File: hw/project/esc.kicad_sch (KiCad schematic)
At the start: 0 parts

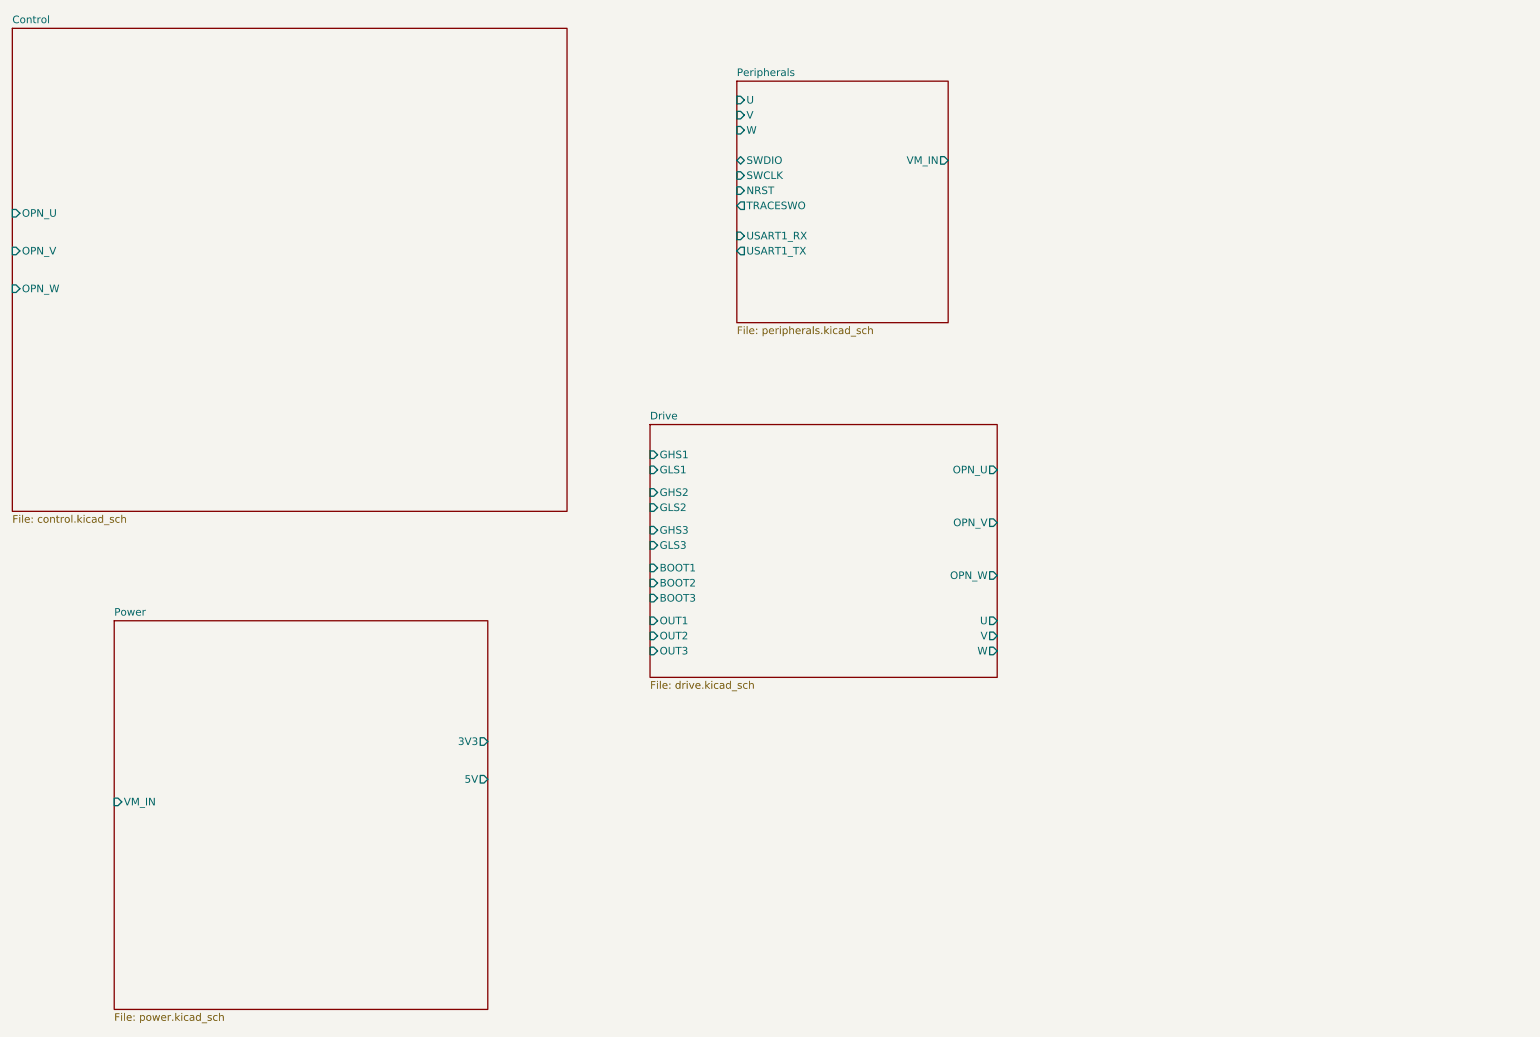
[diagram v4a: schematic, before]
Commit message: added peripherals main sheet and fixed erc errors
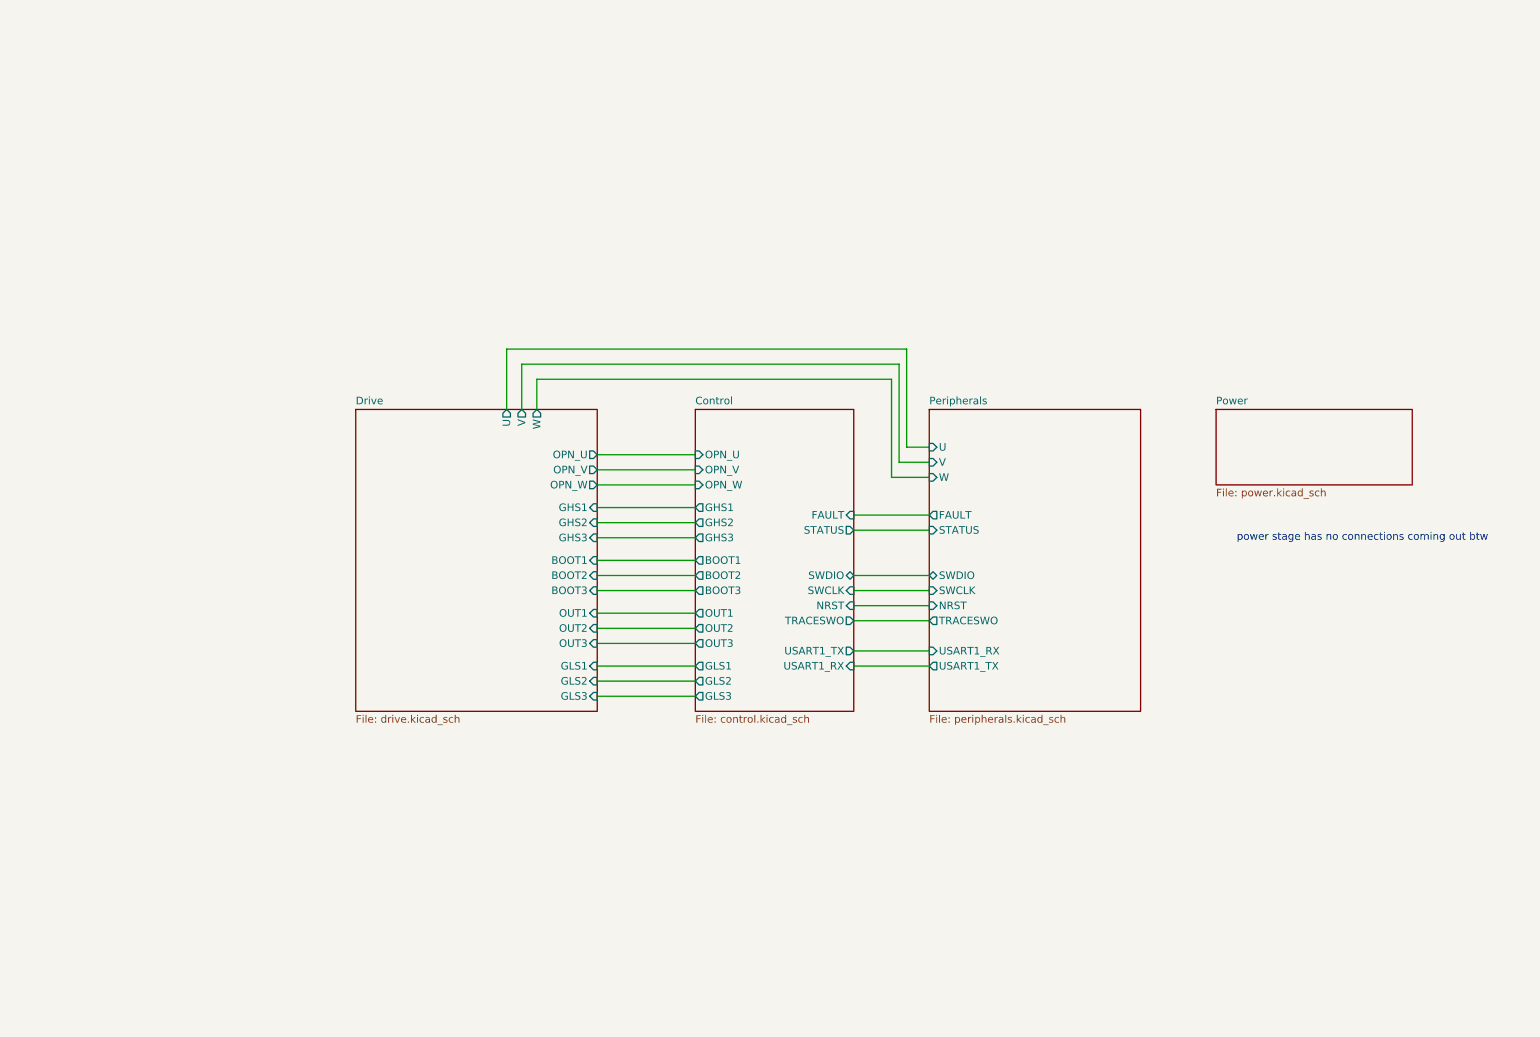
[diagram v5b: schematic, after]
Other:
- sheet Control ports: added BOOT1, BOOT2, BOOT3, FAULT, GHS1, GHS2, GHS3, GLS1, GLS2, GLS3, NRST, OUT1, OUT2, OUT3, STATUS, SWCLK, SWDIO, TRACESWO, USART1_RX, USART1_TX; removed none
- sheet Peripherals ports: added FAULT, STATUS; removed VM_IN
- sheet Power ports: added none; removed 3V3, 5V, VM_IN
- note added: "power stage has no connections coming out btw"

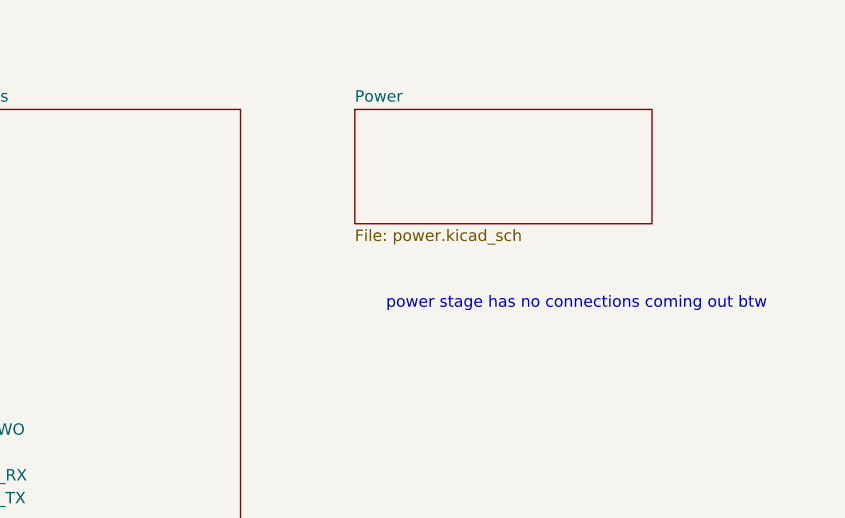
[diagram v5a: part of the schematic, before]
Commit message: Distinguish between hierarchical VM_IN and global VM
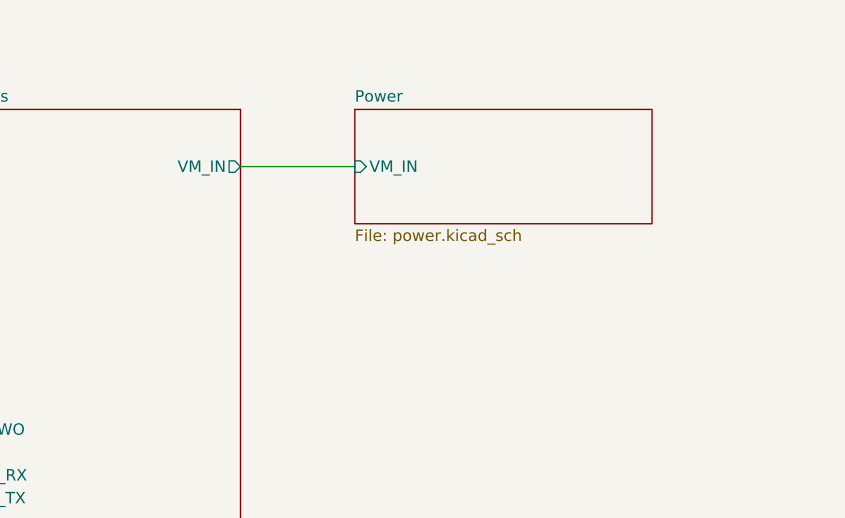
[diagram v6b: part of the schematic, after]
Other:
- sheet Peripherals ports: added VM_IN; removed none
- sheet Power ports: added VM_IN; removed none
- note removed: "power stage has no connections coming out btw"
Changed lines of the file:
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@@
 	(generator_version "10.0")
 	(paper "A4")
-	(text "power stage has no connections coming out btw"
-		(exclude_from_sim no)
-		(at 240.538 101.6 0)
-		(effects
-			(font
-				(size 1.27 1.27)
-			)
-		)
-	)
 	(wire
 		(pts
@@
 		(pts
 			(xy 163.83 69.85) (xy 163.83 86.36)
+		)
+		(stroke
+			(width 0)
+			(type default)
+		)
+	)
+	(wire
+		(pts
+			(xy 203.2 86.36) (xy 215.9 86.36)
 		)
 		(stroke
@@
 			)
 		)
+		(pin "VM_IN" input
+			(at 215.9 86.36 180)
+			(effects
+				(font
+					(size 1.27 1.27)
+				)
+				(justify left)
+			)
+		)
 		(instances
 			(project "esc"
@@
 			)
 		)
+		(pin "VM_IN" output
+			(at 203.2 86.36 0)
+			(effects
+				(font
+					(size 1.27 1.27)
+				)
+				(justify right)
+			)
+		)

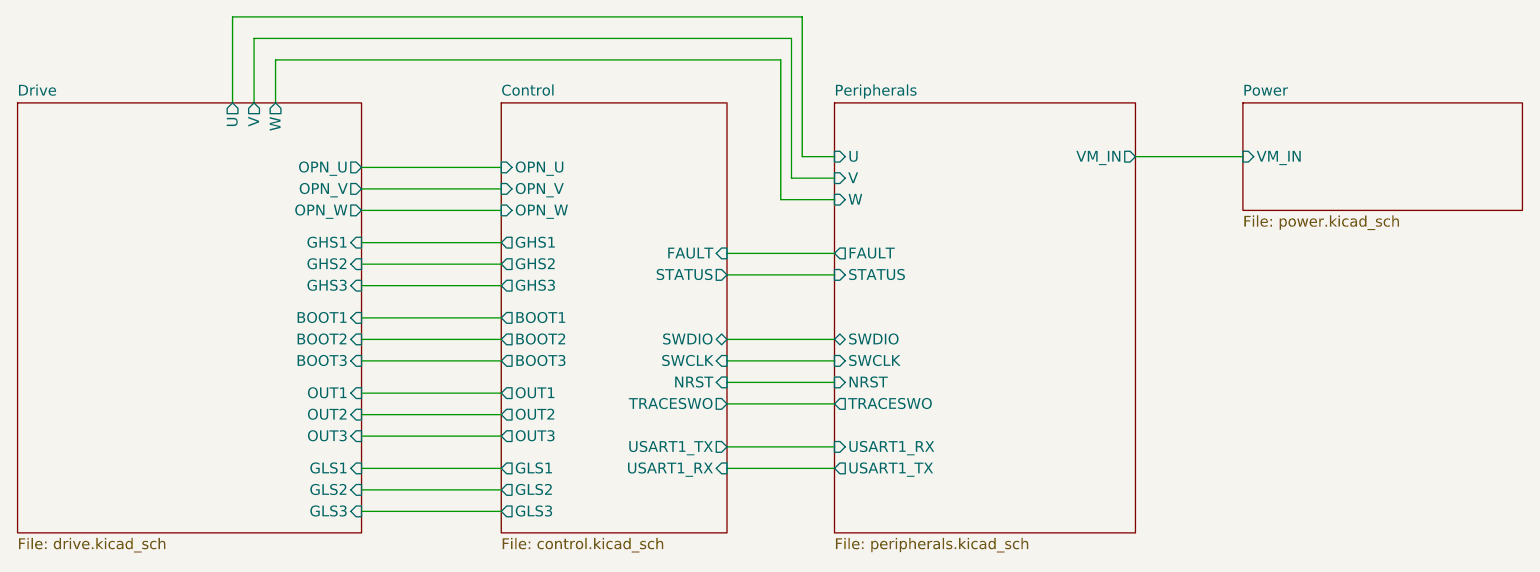
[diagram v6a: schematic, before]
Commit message: Remove spec'd diodes and replace with original suggested parts
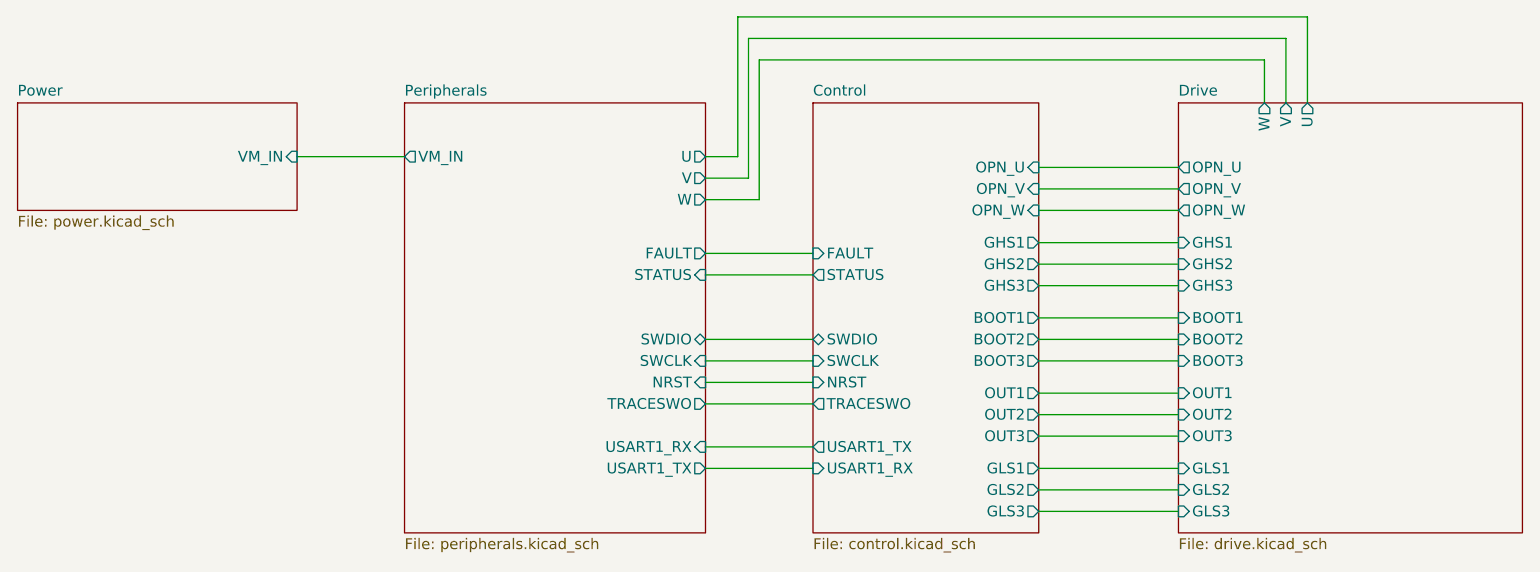
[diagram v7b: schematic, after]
